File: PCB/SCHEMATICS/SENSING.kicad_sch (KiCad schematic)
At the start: 24 parts, among them U3 LTR-303ALS-01, U5 LTR-303ALS-01

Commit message: Added footprints
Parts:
- C4, C5: footprint (none) -> 1UF:CAPC2012X140N
- C6: footprint (none) -> 0ohm:RESC1005X40N; PART  C4177 -> C17168; Unit Price 0.0012 -> 0.0005
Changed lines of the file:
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@@
       (effects (font (size 1.27 1.27)))
     )
-    (property "Footprint" "" (at 113.03 99.3648 0)
+    (property "Footprint" "1UF:CAPC2012X140N" (at 113.03 99.3648 0)
       (effects (font (size 1.27 1.27)) hide)
     )
@@
       (effects (font (size 1.27 1.27)))
     )
-    (property "Footprint" "" (at 212.725 58.42 0)
+    (property "Footprint" "0ohm:RESC1005X40N" (at 212.725 58.42 0)
       (effects (font (size 1.27 1.27)) hide)
     )
@@
       (effects (font (size 1.27 1.27)) hide)
     )
-    (property "PART " "    C4177" (at 212.725 58.42 0)
-      (effects (font (size 1.27 1.27)) hide)
-    )
-    (property "Unit Price" "0.0012" (at 212.725 58.42 0)
+    (property "PART " "C17168" (at 212.725 58.42 0)
+      (effects (font (size 1.27 1.27)) hide)
+    )
+    (property "Unit Price" "0.0005" (at 212.725 58.42 0)
       (effects (font (size 1.27 1.27)) hide)
     )
@@
       (effects (font (size 1.27 1.27)))
     )
-    (property "Footprint" "" (at 41.91 63.5 0)
+    (property "Footprint" "0ohm:RESC1005X40N" (at 41.91 63.5 0)
       (effects (font (size 1.27 1.27)) hide)
     )
@@
       (effects (font (size 1.27 1.27)) hide)
     )
-    (property "PART " "    C4177" (at 41.91 63.5 0)
-      (effects (font (size 1.27 1.27)) hide)
-    )
-    (property "Unit Price" "0.0012" (at 41.91 63.5 0)
+    (property "PART " "C17168" (at 41.91 63.5 0)
+      (effects (font (size 1.27 1.27)) hide)
+    )
+    (property "Unit Price" "0.0005" (at 41.91 63.5 0)
       (effects (font (size 1.27 1.27)) hide)
     )
@@
       (effects (font (size 1.27 1.27)))
     )
-    (property "Footprint" "" (at 119.38 51.1048 0)
+    (property "Footprint" "1UF:CAPC2012X140N" (at 119.38 51.1048 0)
       (effects (font (size 1.27 1.27)) hide)
     )
@@
       (effects (font (size 1.27 1.27)))
     )
-    (property "Footprint" "" (at 41.91 68.58 0)
+    (property "Footprint" "0ohm:RESC1005X40N" (at 41.91 68.58 0)
       (effects (font (size 1.27 1.27)) hide)
     )
@@
       (effects (font (size 1.27 1.27)) hide)
     )
-    (property "PART " "    C4177" (at 41.91 68.58 0)
-      (effects (font (size 1.27 1.27)) hide)
-    )
-    (property "Unit Price" "0.0012" (at 41.91 68.58 0)
-      (effects (font (size 1.27 1.27)) hide)
-    )
+    (property "PART " "C17168" (at 41.91 68.58 0)
+      (effects (font (size 1.27 1.27)) hide)
+    )
+    (property "Unit Price" "0.0005" (at 41.91 68.58 0)
+      (effects (font (size 1.27 1.27)) hide)
+    )

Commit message: updated schematics and footprints
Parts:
- C6: PART  C17168 -> C17168
- R18, R19, R20, R21: footprint (none) -> footprint:R0402
- R22, R23: footprint (none) -> footprint:R1206
- U3, U5: footprint OptoDevice:Lite-On_LTR-303ALS-01 -> footprint:SOT-363_L2.0-W1.3-P0.65-LS2.1-BL
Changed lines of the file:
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@@
       (effects (font (size 1.27 1.27)) (justify left))
     )
-    (property "Footprint" "" (at 60.96 57.15 0)
+    (property "Footprint" "footprint:R0402" (at 60.96 57.15 0)
       (effects (font (size 1.27 1.27)) hide)
     )
@@
       (effects (font (size 1.27 1.27)) (justify left))
     )
-    (property "Footprint" "" (at 78.74 105.41 0)
+    (property "Footprint" "footprint:R0402" (at 78.74 105.41 0)
       (effects (font (size 1.27 1.27)) hide)
     )
@@
       (effects (font (size 1.27 1.27)) (justify left))
     )
-    (property "Footprint" "" (at 69.85 57.15 0)
+    (property "Footprint" "footprint:R0402" (at 69.85 57.15 0)
       (effects (font (size 1.27 1.27)) hide)
     )
@@
       (effects (font (size 1.27 1.27)) hide)
     )
-    (property "PART " "C17168" (at 212.725 58.42 0)
+    (property "PART " "   C17168" (at 212.725 58.42 0)
       (effects (font (size 1.27 1.27)) hide)
     )
@@
       (effects (font (size 1.27 1.27)) (justify left))
     )
-    (property "Footprint" "" (at 87.63 105.41 0)
+    (property "Footprint" "footprint:R0402" (at 87.63 105.41 0)
       (effects (font (size 1.27 1.27)) hide)
     )
@@
       (effects (font (size 1.27 1.27)) hide)
     )
-    (property "PART " "C17168" (at 41.91 63.5 0)
+    (property "PART " "   C17168" (at 41.91 63.5 0)
       (effects (font (size 1.27 1.27)) hide)
     )
@@
       (effects (font (size 1.27 1.27)) (justify right))
     )
-    (property "Footprint" "" (at 195.58 53.34 0)
+    (property "Footprint" "footprint:R1206" (at 195.58 53.34 0)
       (effects (font (size 1.27 1.27)) hide)
     )
@@
       (effects (font (size 1.27 1.27)) (justify right))
     )
-    (property "Footprint" "" (at 195.58 63.5 0)
+    (property "Footprint" "footprint:R1206" (at 195.58 63.5 0)
       (effects (font (size 1.27 1.27)) hide)
     )
@@
       (effects (font (size 1.27 1.27)) hide)
     )
-    (property "PART " "C17168" (at 41.91 68.58 0)
+    (property "PART " "   C17168" (at 41.91 68.58 0)
       (effects (font (size 1.27 1.27)) hide)
     )
@@
       (effects (font (size 1.27 1.27)))
     )
-    (property "Footprint" "OptoDevice:Lite-On_LTR-303ALS-01" (at 124.46 54.61 0)
+    (property "Footprint" "footprint:SOT-363_L2.0-W1.3-P0.65-LS2.1-BL" (at 124.46 54.61 0)
       (effects (font (size 1.27 1.27)) hide)
     )
@@
       (effects (font (size 1.27 1.27)))
     )
-    (property "Footprint" "OptoDevice:Lite-On_LTR-303ALS-01" (at 118.11 102.87 0)
-      (effects (font (size 1.27 1.27)) hide)
-    )
+    (property "Footprint" "footprint:SOT-363_L2.0-W1.3-P0.65-LS2.1-BL" (at 118.11 102.87 0)
+      (effects (font (size 1.27 1.27)) hide)
+    )

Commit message: Fixed ercs
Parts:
- TP1, TP13, TP14, TP15, TP16, TP17, TP18, TP19, TP2, TP20, TP21: footprint (none) -> TestPoint:TestPoint_Bridge_Pitch2.0mm_Drill0.7mm
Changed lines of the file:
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@@
       (effects (font (size 1.27 1.27)))
     )
-    (property "Footprint" "" (at 66.04 106.68 0)
+    (property "Footprint" "TestPoint:TestPoint_Bridge_Pitch2.0mm_Drill0.7mm" (at 66.04 106.68 0)
       (effects (font (size 1.27 1.27)) hide)
     )
@@
       (effects (font (size 1.27 1.27)) (justify left))
     )
-    (property "Footprint" "" (at 60.96 40.64 0)
+    (property "Footprint" "TestPoint:TestPoint_Bridge_Pitch2.0mm_Drill0.7mm" (at 60.96 40.64 0)
       (effects (font (size 1.27 1.27)) hide)
     )
@@
       (effects (font (size 1.27 1.27)) (justify left))
     )
-    (property "Footprint" "" (at 88.9 93.98 0)
+    (property "Footprint" "TestPoint:TestPoint_Bridge_Pitch2.0mm_Drill0.7mm" (at 88.9 93.98 0)
       (effects (font (size 1.27 1.27)) hide)
     )
@@
       (effects (font (size 1.27 1.27)))
     )
-    (property "Footprint" "" (at 66.04 111.76 0)
+    (property "Footprint" "TestPoint:TestPoint_Bridge_Pitch2.0mm_Drill0.7mm" (at 66.04 111.76 0)
       (effects (font (size 1.27 1.27)) hide)
     )
@@
       (effects (font (size 1.27 1.27)) (justify left))
     )
-    (property "Footprint" "" (at 88.9 45.72 0)
+    (property "Footprint" "TestPoint:TestPoint_Bridge_Pitch2.0mm_Drill0.7mm" (at 88.9 45.72 0)
       (effects (font (size 1.27 1.27)) hide)
     )
@@
       (effects (font (size 1.27 1.27)) (justify left))
     )
-    (property "Footprint" "" (at 210.82 41.91 0)
+    (property "Footprint" "TestPoint:TestPoint_Bridge_Pitch2.0mm_Drill0.7mm" (at 210.82 41.91 0)
       (effects (font (size 1.27 1.27)) hide)
     )
@@
       (effects (font (size 1.27 1.27)) (justify left))
     )
-    (property "Footprint" "" (at 134.62 43.18 0)
+    (property "Footprint" "TestPoint:TestPoint_Bridge_Pitch2.0mm_Drill0.7mm" (at 134.62 43.18 0)
       (effects (font (size 1.27 1.27)) hide)
     )
@@
       (effects (font (size 1.27 1.27)) (justify left))
     )
-    (property "Footprint" "" (at 57.15 48.26 0)
+    (property "Footprint" "TestPoint:TestPoint_Bridge_Pitch2.0mm_Drill0.7mm" (at 57.15 48.26 0)
       (effects (font (size 1.27 1.27)) hide)
     )
@@
       (effects (font (size 1.27 1.27)) (justify left))
     )
-    (property "Footprint" "" (at 118.11 105.41 0)
+    (property "Footprint" "TestPoint:TestPoint_Bridge_Pitch2.0mm_Drill0.7mm" (at 118.11 105.41 0)
       (effects (font (size 1.27 1.27)) hide)
     )
@@
       (effects (font (size 1.27 1.27)) (justify right))
     )
-    (property "Footprint" "" (at 199.39 67.31 0)
+    (property "Footprint" "TestPoint:TestPoint_Bridge_Pitch2.0mm_Drill0.7mm" (at 199.39 67.31 0)
       (effects (font (size 1.27 1.27)) hide)
     )
@@
       (effects (font (size 1.27 1.27)) (justify left))
     )
-    (property "Footprint" "" (at 97.79 44.45 0)
-      (effects (font (size 1.27 1.27)) hide)
-    )
+    (property "Footprint" "TestPoint:TestPoint_Bridge_Pitch2.0mm_Drill0.7mm" (at 97.79 44.45 0)
+      (effects (font (size 1.27 1.27)) hide)
+    )

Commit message: Fixing ERCs
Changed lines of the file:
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@@
     (effects (font (size 1.27 1.27)) (justify left))
   )
-  (hierarchical_label "3V3" (shape input) (at 134.62 52.07 0) (fields_autoplaced)
+  (hierarchical_label "3V3" (shape output) (at 134.62 52.07 0) (fields_autoplaced)
     (effects (font (size 1.27 1.27)) (justify left))
   )

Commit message: Started PCB design
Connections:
- net Earth is gone; now on net GND: C4.1, C5.1, R23.1, U3.3 (GND), U5.3 (GND)

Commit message: updated path for footprints
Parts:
- C4, C5: footprint 1UF:CAPC2012X140N -> footprint:CAPC2012X140N
- C6: footprint 0ohm:RESC1005X40N -> footprint:RESC1005X40N
- TP1, TP13, TP14, TP15, TP16, TP17, TP18, TP19, TP2, TP20, TP21: footprint TestPoint:TestPoint_Bridge_Pitch2.0mm_Drill0.7mm -> TestPoint:TestPoint_Pad_D2.0mm
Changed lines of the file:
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@@
       (effects (font (size 1.27 1.27)))
     )
-    (property "Footprint" "1UF:CAPC2012X140N" (at 113.03 99.3648 0)
+    (property "Footprint" "footprint:CAPC2012X140N" (at 113.03 99.3648 0)
       (effects (font (size 1.27 1.27)) hide)
     )
@@
       (effects (font (size 1.27 1.27)))
     )
-    (property "Footprint" "TestPoint:TestPoint_Bridge_Pitch2.0mm_Drill0.7mm" (at 66.04 106.68 0)
+    (property "Footprint" "TestPoint:TestPoint_Pad_D2.0mm" (at 66.04 106.68 0)
       (effects (font (size 1.27 1.27)) hide)
     )
@@
       (effects (font (size 1.27 1.27)) (justify left))
     )
-    (property "Footprint" "TestPoint:TestPoint_Bridge_Pitch2.0mm_Drill0.7mm" (at 60.96 40.64 0)
+    (property "Footprint" "TestPoint:TestPoint_Pad_D2.0mm" (at 60.96 40.64 0)
       (effects (font (size 1.27 1.27)) hide)
     )
@@
       (effects (font (size 1.27 1.27)) (justify left))
     )
-    (property "Footprint" "TestPoint:TestPoint_Bridge_Pitch2.0mm_Drill0.7mm" (at 88.9 93.98 0)
+    (property "Footprint" "TestPoint:TestPoint_Pad_D2.0mm" (at 88.9 93.98 0)
       (effects (font (size 1.27 1.27)) hide)
     )
@@
       (effects (font (size 1.27 1.27)))
     )
-    (property "Footprint" "TestPoint:TestPoint_Bridge_Pitch2.0mm_Drill0.7mm" (at 66.04 111.76 0)
+    (property "Footprint" "TestPoint:TestPoint_Pad_D2.0mm" (at 66.04 111.76 0)
       (effects (font (size 1.27 1.27)) hide)
     )
@@
       (effects (font (size 1.27 1.27)) (justify left))
     )
-    (property "Footprint" "TestPoint:TestPoint_Bridge_Pitch2.0mm_Drill0.7mm" (at 88.9 45.72 0)
+    (property "Footprint" "TestPoint:TestPoint_Pad_D2.0mm" (at 88.9 45.72 0)
       (effects (font (size 1.27 1.27)) hide)
     )
@@
       (effects (font (size 1.27 1.27)))
     )
-    (property "Footprint" "0ohm:RESC1005X40N" (at 212.725 58.42 0)
+    (property "Footprint" "footprint:RESC1005X40N" (at 212.725 58.42 0)
       (effects (font (size 1.27 1.27)) hide)
     )
@@
       (effects (font (size 1.27 1.27)) (justify left))
     )
-    (property "Footprint" "TestPoint:TestPoint_Bridge_Pitch2.0mm_Drill0.7mm" (at 210.82 41.91 0)
+    (property "Footprint" "TestPoint:TestPoint_Pad_D2.0mm" (at 210.82 41.91 0)
       (effects (font (size 1.27 1.27)) hide)
     )
@@
       (effects (font (size 1.27 1.27)) (justify left))
     )
-    (property "Footprint" "TestPoint:TestPoint_Bridge_Pitch2.0mm_Drill0.7mm" (at 134.62 43.18 0)
+    (property "Footprint" "TestPoint:TestPoint_Pad_D2.0mm" (at 134.62 43.18 0)
       (effects (font (size 1.27 1.27)) hide)
     )
@@
       (effects (font (size 1.27 1.27)) (justify left))
     )
-    (property "Footprint" "TestPoint:TestPoint_Bridge_Pitch2.0mm_Drill0.7mm" (at 57.15 48.26 0)
+    (property "Footprint" "TestPoint:TestPoint_Pad_D2.0mm" (at 57.15 48.26 0)
       (effects (font (size 1.27 1.27)) hide)
     )
@@
       (effects (font (size 1.27 1.27)) (justify left))
     )
-    (property "Footprint" "TestPoint:TestPoint_Bridge_Pitch2.0mm_Drill0.7mm" (at 118.11 105.41 0)
+    (property "Footprint" "TestPoint:TestPoint_Pad_D2.0mm" (at 118.11 105.41 0)
       (effects (font (size 1.27 1.27)) hide)
     )
@@
       (effects (font (size 1.27 1.27)))
     )
-    (property "Footprint" "0ohm:RESC1005X40N" (at 41.91 63.5 0)
+    (property "Footprint" "footprint:RESC1005X40N" (at 41.91 63.5 0)
       (effects (font (size 1.27 1.27)) hide)
     )
@@
       (effects (font (size 1.27 1.27)))
     )
-    (property "Footprint" "1UF:CAPC2012X140N" (at 119.38 51.1048 0)
+    (property "Footprint" "footprint:CAPC2012X140N" (at 119.38 51.1048 0)
       (effects (font (size 1.27 1.27)) hide)
     )
@@
       (effects (font (size 1.27 1.27)))
     )
-    (property "Footprint" "0ohm:RESC1005X40N" (at 41.91 68.58 0)
+    (property "Footprint" "footprint:RESC1005X40N" (at 41.91 68.58 0)
       (effects (font (size 1.27 1.27)) hide)
     )
@@
       (effects (font (size 1.27 1.27)) (justify right))
     )
-    (property "Footprint" "TestPoint:TestPoint_Bridge_Pitch2.0mm_Drill0.7mm" (at 199.39 67.31 0)
+    (property "Footprint" "TestPoint:TestPoint_Pad_D2.0mm" (at 199.39 67.31 0)
       (effects (font (size 1.27 1.27)) hide)
     )
@@
       (effects (font (size 1.27 1.27)) (justify left))
     )
-    (property "Footprint" "TestPoint:TestPoint_Bridge_Pitch2.0mm_Drill0.7mm" (at 97.79 44.45 0)
-      (effects (font (size 1.27 1.27)) hide)
-    )
+    (property "Footprint" "TestPoint:TestPoint_Pad_D2.0mm" (at 97.79 44.45 0)
+      (effects (font (size 1.27 1.27)) hide)
+    )

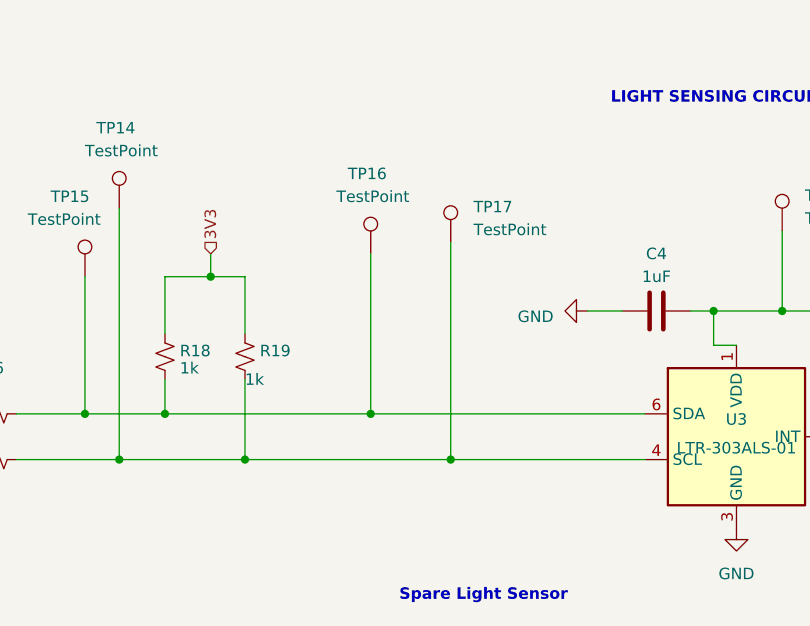
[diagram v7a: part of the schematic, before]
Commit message: Added traces
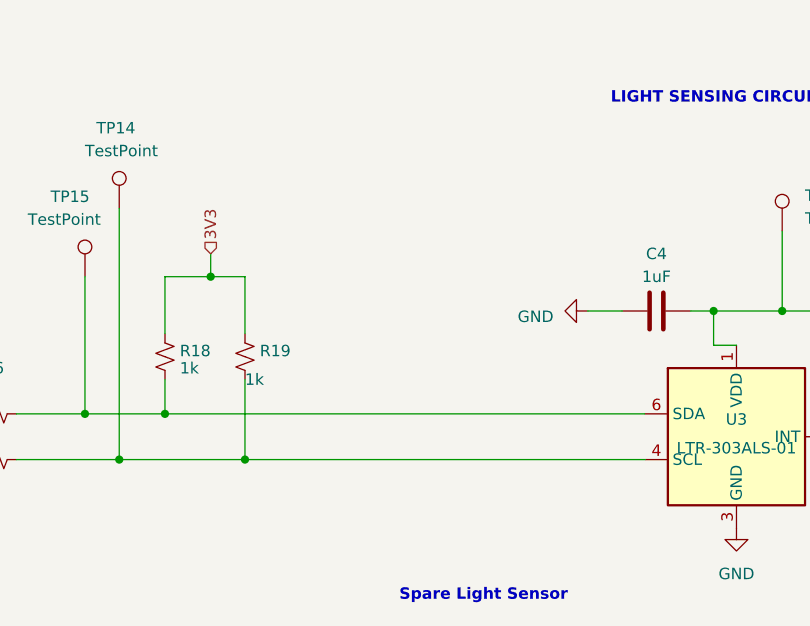
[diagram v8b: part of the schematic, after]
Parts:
- removed TP16, TP17: TestPoint, TestPoint:TestPoint_Pad_D2.0mm, symbol Connector:TestPoint
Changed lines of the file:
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@@
   (junction (at 78.74 111.76) (diameter 0) (color 0 0 0 0)
   )
-  (junction (at 92.71 68.58) (diameter 0) (color 0 0 0 0)
-  )
   (junction (at 129.54 52.07) (diameter 0) (color 0 0 0 0)
   )
   (junction (at 55.88 68.58) (diameter 0) (color 0 0 0 0)
   )
-  (junction (at 83.82 63.5) (diameter 0) (color 0 0 0 0)
-  )
   (junction (at 195.58 58.42) (diameter 0) (color 0 0 0 0)
   )
@@
     (stroke (width 0) (type default))
   )
-  (wire (pts (xy 92.71 68.58) (xy 114.3 68.58))
+  (wire (pts (xy 69.85 68.58) (xy 114.3 68.58))
     (stroke (width 0) (type default))
   )
@@
     (stroke (width 0) (type default))
   )
-  (wire (pts (xy 83.82 45.72) (xy 83.82 63.5))
-    (stroke (width 0) (type default))
-  )
   (wire (pts (xy 134.62 114.3) (xy 128.27 114.3))
     (stroke (width 0) (type default))
@@
     (stroke (width 0) (type default))
   )
-  (wire (pts (xy 92.71 44.45) (xy 92.71 68.58))
-    (stroke (width 0) (type default))
-  )
   (wire (pts (xy 113.03 100.33) (xy 115.57 100.33))
     (stroke (width 0) (type default))
@@
     (stroke (width 0) (type default))
   )
-  (wire (pts (xy 69.85 68.58) (xy 92.71 68.58))
-    (stroke (width 0) (type default))
-  )
   (wire (pts (xy 124.46 55.88) (xy 121.92 55.88))
     (stroke (width 0) (type default))
@@
     (stroke (width 0) (type default))
   )
-  (wire (pts (xy 83.82 63.5) (xy 114.3 63.5))
-    (stroke (width 0) (type default))
-  )
   (wire (pts (xy 69.85 48.26) (xy 69.85 54.61))
     (stroke (width 0) (type default))
@@
     (stroke (width 0) (type default))
   )
-  (wire (pts (xy 60.96 63.5) (xy 83.82 63.5))
+  (wire (pts (xy 60.96 63.5) (xy 114.3 63.5))
     (stroke (width 0) (type default))
   )
@@
         (path "/c9ca3a5c-30cb-4dce-b611-3270b9f3284b/1428f64b-a76f-4ab8-8617-b5b39829c481"
           (reference "TP2") (unit 1)
-        )
-      )
-    )
-  )
-  (symbol (lib_id "Connector:TestPoint") (at 83.82 45.72 0) (unit 1)
-    (in_bom yes) (on_board yes) (dnp no)
-    (property "Reference" "TP16" (at 81.28 36.83 0)
-      (effects (font (size 1.27 1.27)) (justify left))
-    )
-    (property "Value" "TestPoint" (at 80.01 39.37 0)
-      (effects (font (size 1.27 1.27)) (justify left))
-    )
-    (property "Footprint" "TestPoint:TestPoint_Pad_D2.0mm" (at 88.9 45.72 0)
-      (effects (font (size 1.27 1.27)) hide)
-    )
-    (property "Datasheet" "~" (at 88.9 45.72 0)
-      (effects (font (size 1.27 1.27)) hide)
-    )
-    (property "PART " "    TP16" (at 83.82 45.72 0)
-      (effects (font (size 1.27 1.27)) hide)
-    )
-    (pin "1")
-    (instances
-      (project "SCHEMATICS"
-        (path "/c9ca3a5c-30cb-4dce-b611-3270b9f3284b/1428f64b-a76f-4ab8-8617-b5b39829c481"
-          (reference "TP16") (unit 1)
         )
       )
@@
         )
       )
-    )
-  )
-  (symbol (lib_id "Connector:TestPoint") (at 92.71 44.45 0) (unit 1)
-    (in_bom yes) (on_board yes) (dnp no) (fields_autoplaced)
-    (property "Reference" "TP17" (at 95.25 40.513 0)
-      (effects (font (size 1.27 1.27)) (justify left))
-    )
-    (property "Value" "TestPoint" (at 95.25 43.053 0)
-      (effects (font (size 1.27 1.27)) (justify left))
-    )
-    (property "Footprint" "TestPoint:TestPoint_Pad_D2.0mm" (at 97.79 44.45 0)
-      (effects (font (size 1.27 1.27)) hide)
-    )
-    (property "Datasheet" "~" (at 97.79 44.45 0)
-      (effects (font (size 1.27 1.27)) hide)
-    )
-    (property "PART " "    TP17" (at 92.71 44.45 0)
-      (effects (font (size 1.27 1.27)) hide)
-    )
-    (pin "1")
-    (instances
-      (project "SCHEMATICS"
-        (path "/c9ca3a5c-30cb-4dce-b611-3270b9f3284b/1428f64b-a76f-4ab8-8617-b5b39829c481"
-          (reference "TP17") (unit 1)
-        )
-      )
